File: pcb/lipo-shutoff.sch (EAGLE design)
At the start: 10 parts, among them Q1 AON6411, SW1 FSM4JSMA, U1 LT6703-2

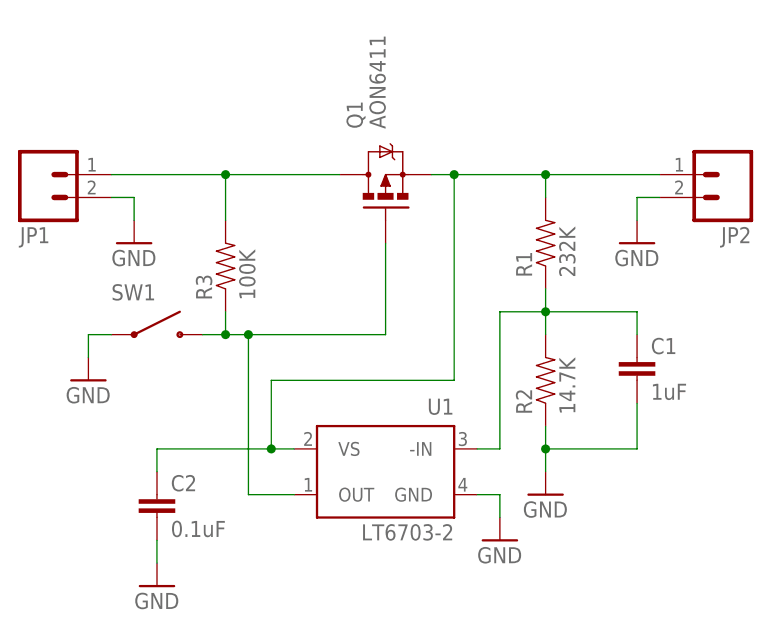
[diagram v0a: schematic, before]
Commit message: Fixed lipo cutoff board
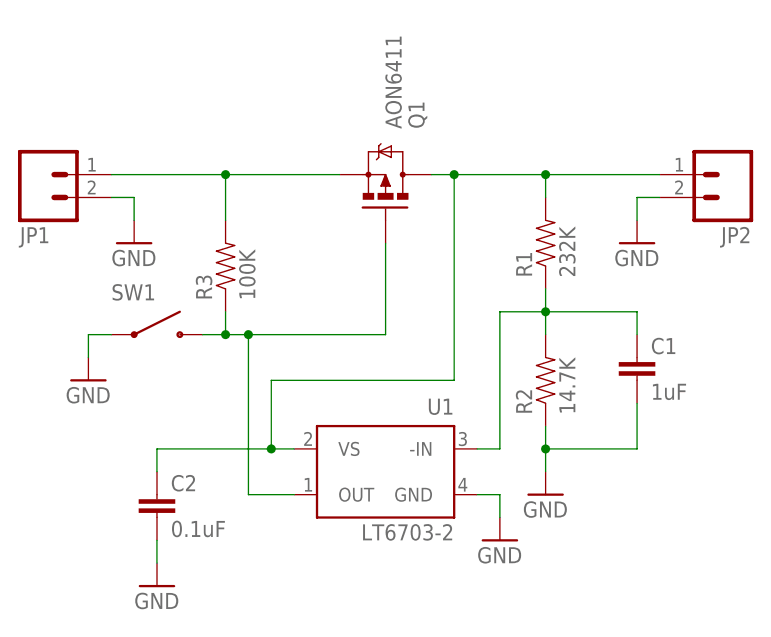
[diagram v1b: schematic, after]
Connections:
- net N$1: now also Q1.S; no longer Q1.D
- net N$4: now also Q1.D; no longer Q1.S
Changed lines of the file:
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@@
 </plain>
 <instances>
-<instance part="Q1" gate="G$1" x="48.26" y="25.4" rot="R90"/>
+<instance part="Q1" gate="G$1" x="48.26" y="25.4" rot="MR90"/>
 <instance part="U1" gate="G$1" x="48.26" y="-7.62" rot="MR0"/>
 <instance part="GND1" gate="1" x="66.04" y="-10.16"/>
@@
 <segment>
 <pinref part="JP1" gate="G$1" pin="1"/>
-<pinref part="Q1" gate="G$1" pin="D"/>
 <wire x1="17.78" y1="25.4" x2="30.48" y2="25.4" width="0.1524" layer="91"/>
 <pinref part="R3" gate="G$1" pin="2"/>
+<wire x1="30.48" y1="25.4" x2="30.48" y2="20.32" width="0.1524" layer="91"/>
+<pinref part="Q1" gate="G$1" pin="S"/>
 <wire x1="30.48" y1="25.4" x2="43.18" y2="25.4" width="0.1524" layer="91"/>
-<wire x1="30.48" y1="25.4" x2="30.48" y2="20.32" width="0.1524" layer="91"/>
 <junction x="30.48" y="25.4"/>
 </segment>
@@
 <net name="N$4" class="0">
 <segment>
-<pinref part="Q1" gate="G$1" pin="S"/>
 <wire x1="78.74" y1="25.4" x2="66.04" y2="25.4" width="0.1524" layer="91"/>
 <pinref part="JP2" gate="G$1" pin="1"/>
 <pinref part="U1" gate="G$1" pin="VS"/>
 <wire x1="66.04" y1="25.4" x2="55.88" y2="25.4" width="0.1524" layer="91"/>
-<wire x1="55.88" y1="25.4" x2="53.34" y2="25.4" width="0.1524" layer="91"/>
 <wire x1="38.1" y1="-5.08" x2="35.56" y2="-5.08" width="0.1524" layer="91"/>
 <wire x1="35.56" y1="-5.08" x2="35.56" y2="2.54" width="0.1524" layer="91"/>
@@
 <pinref part="R1" gate="G$1" pin="2"/>
 <wire x1="66.04" y1="22.86" x2="66.04" y2="25.4" width="0.1524" layer="91"/>
-<junction x="55.88" y="25.4"/>
 <junction x="66.04" y="25.4"/>
 <pinref part="C2" gate="G$1" pin="1"/>
@@
 <wire x1="22.86" y1="-5.08" x2="22.86" y2="-7.62" width="0.1524" layer="91"/>
 <junction x="35.56" y="-5.08"/>
+<pinref part="Q1" gate="G$1" pin="D"/>
+<wire x1="53.34" y1="25.4" x2="55.88" y2="25.4" width="0.1524" layer="91"/>
+<junction x="55.88" y="25.4"/>
 </segment>
 </net>
